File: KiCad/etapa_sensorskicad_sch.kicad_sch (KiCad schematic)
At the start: 17 parts, among them J1 Conn_01x04_Pin, J2 Conn_01x04_Pin, K1 Fujitsu_FTR-LYAA005x, K2 Fujitsu_FTR-LYAA005x, Q1 IRLIZ44N, U1 FDC2214

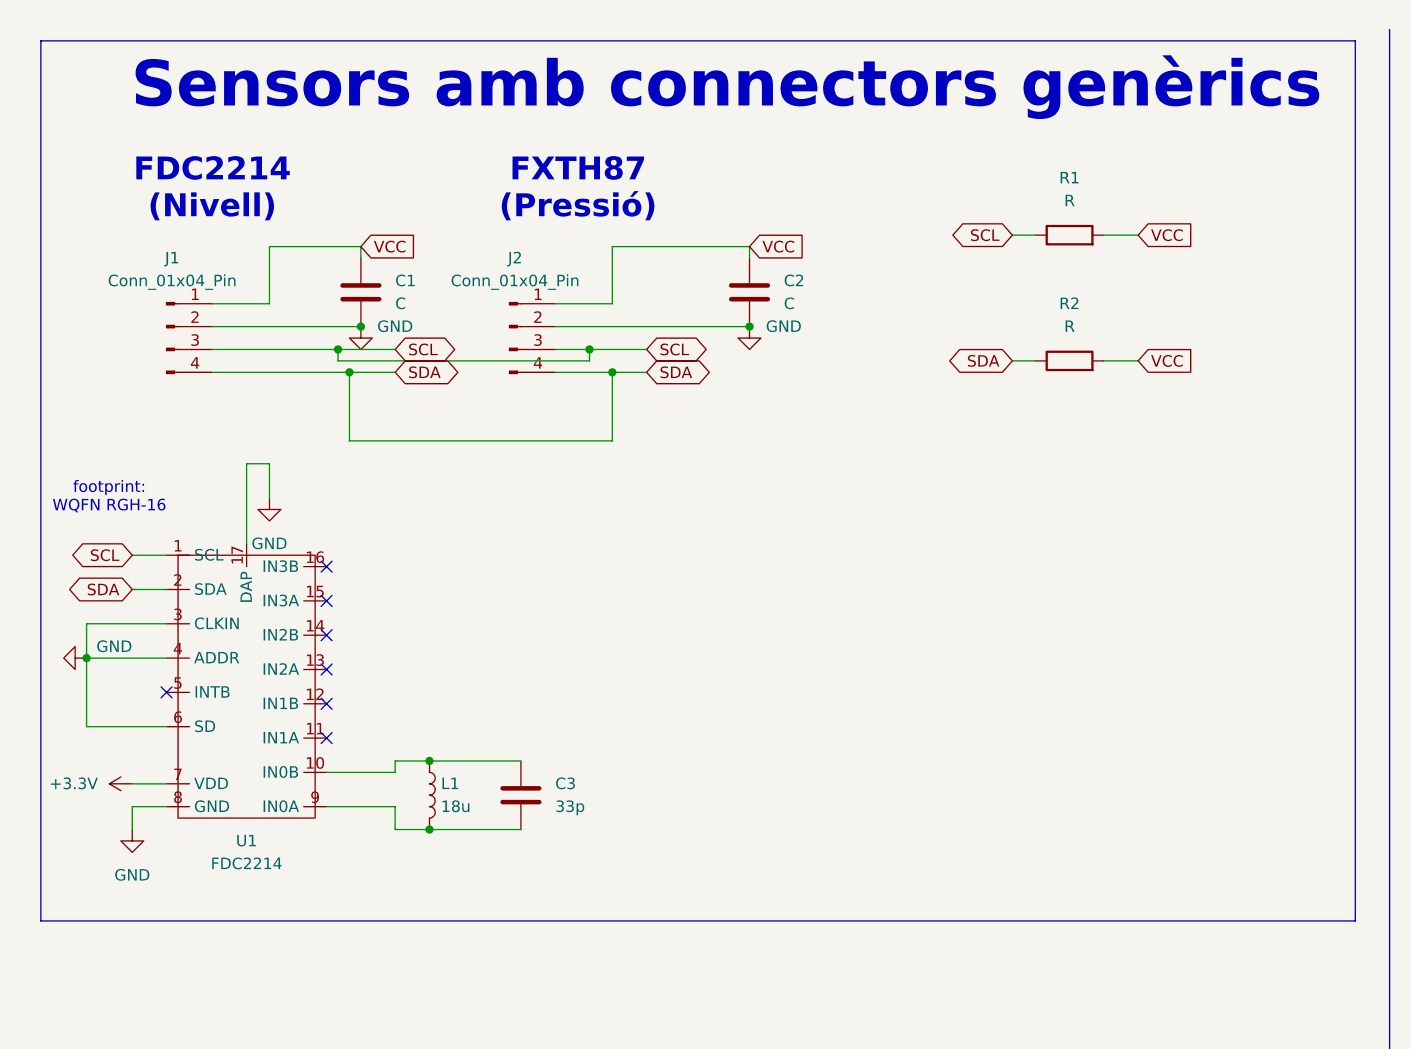
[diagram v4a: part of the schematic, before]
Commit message: Simbol del sensor de pressió creat, amb el seu possible footprint (?). A més, connexions necessàries fetes i eliminació dels connector que hi havien
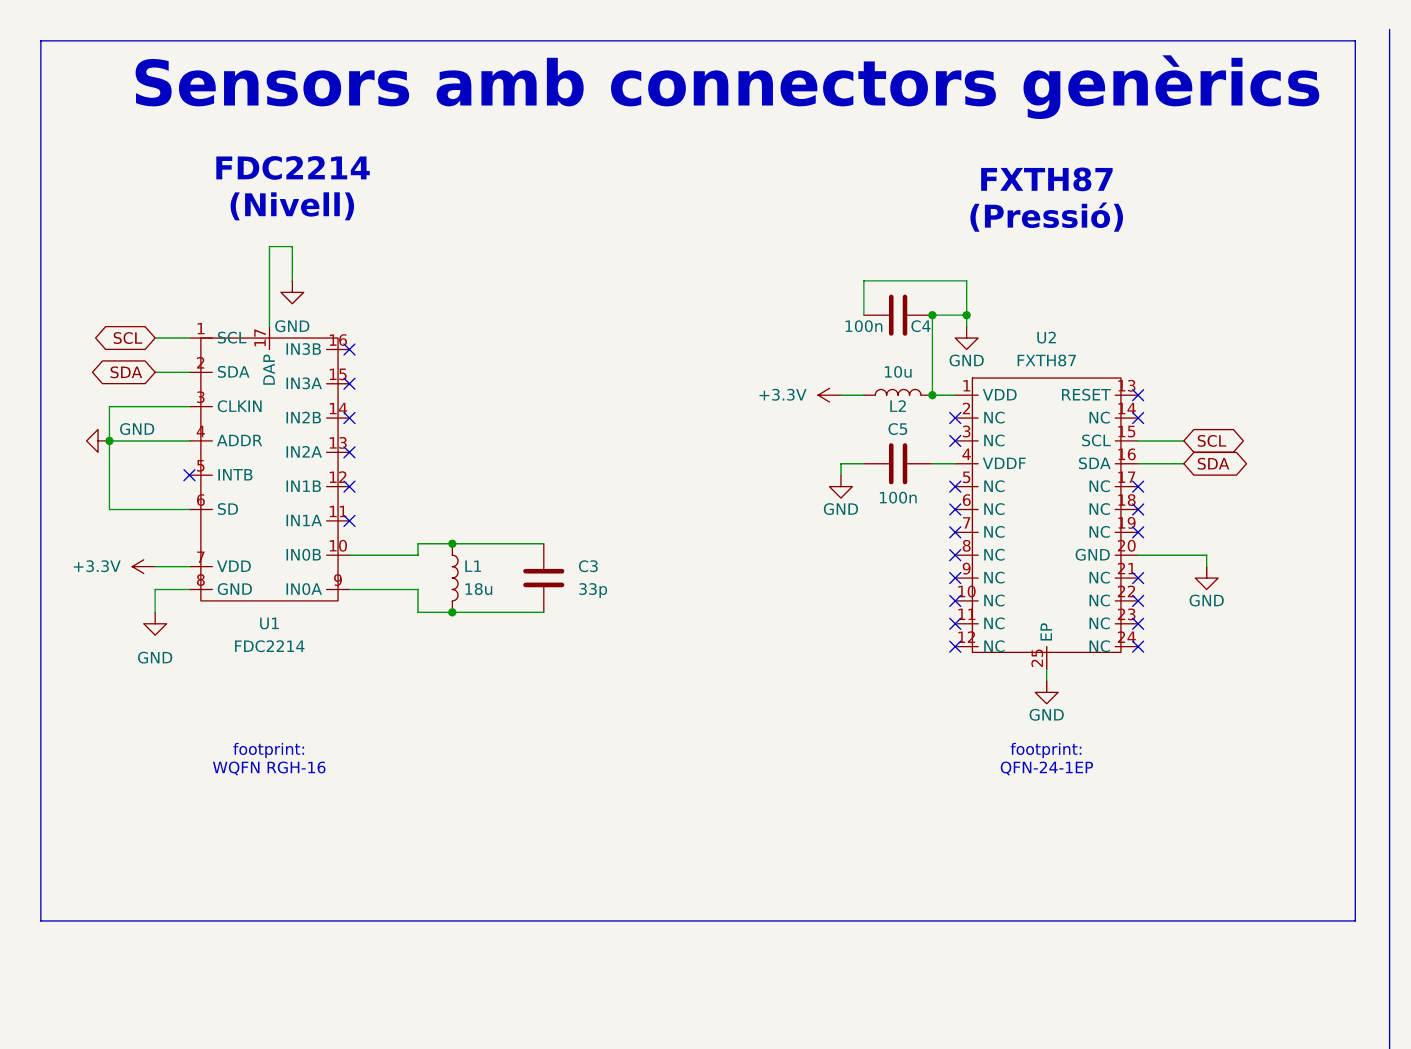
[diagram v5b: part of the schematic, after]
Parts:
- removed C1, C2: C, symbol Device:C
- removed J1, J2: Conn_01x04_Pin, symbol Connector:Conn_01x04_Pin
- removed R1, R2: R, symbol Device:R
- added C4, C5: 100n, symbol Device:C
- added L2: 10u, symbol Device:L
- added U2: FXTH87, symbol Sensors_Custom:FXTH87
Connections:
- net +3.3V: now also L2.1
- net GND: now also C4.1, C4.2, C5.2, L2.2, U2.1 (VDD), U2.20 (GND), U2.25 (EP)
- net SCL: now also U2.15 (SCL)
- net SDA: now also U2.16 (SDA)
- new net: C5.1, U2.4 (VDDF)
- no-connect marks 7 -> 26
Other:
- note added: "footprint: QFN-24-1EP"
- moved on the sheet: C3, L1, U1
